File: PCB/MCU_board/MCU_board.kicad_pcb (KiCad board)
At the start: 4 copper layers, 73 x 73 mm, 51 parts, among them IC1 NEO-F10N-00B, IC2 TXB0104PWR, IC3 ESP32-S3-WROOM-1-N4R8, IC6 4259-63, IC8 MAX98357AETE+T, J1 DS1013-40SSIB1-B-0, J4 FXP612 (u.FL) 2, J5 FXP612 (u.FL) 1, J6 SIM8055-6-1-14-00-A, J7 FXP612 (u.FL) 1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

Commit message: all my pcb
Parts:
- removed C10: CL10B104KO8NNNC, CL10B104KO8NNNC:CAPC1608X90N
- moved C2 0.10 mm to (49.0, 138.3)
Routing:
- net /Stationary/GSM_sheet/SIM_POWER: track 37.0 -> 31.0 mm, vias 3 -> 2
- net GND: track 135.6 -> 134.0 mm, vias 36 -> 35

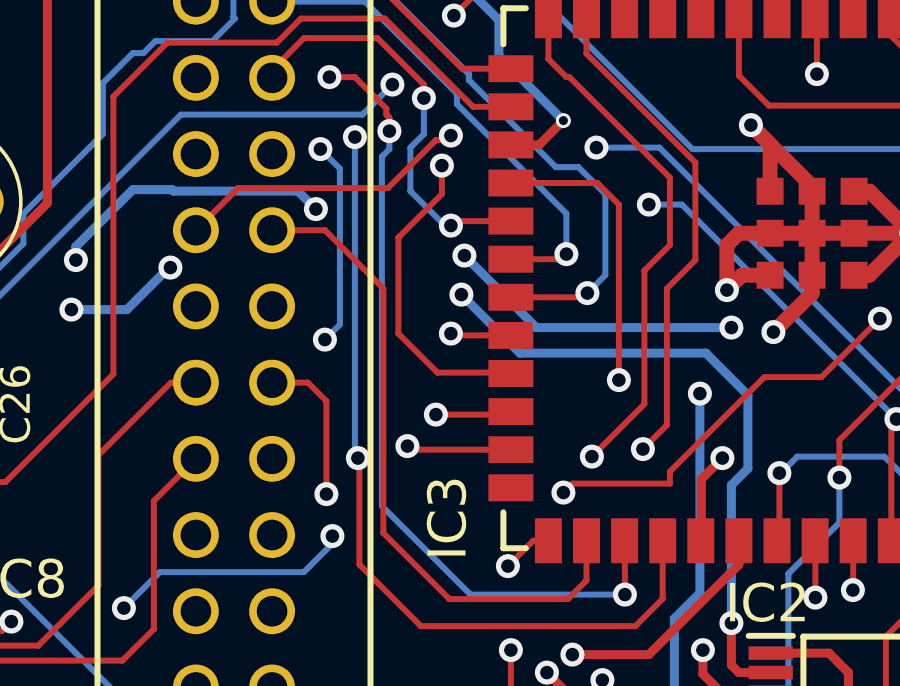
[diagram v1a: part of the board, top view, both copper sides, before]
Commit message: ATA connector updated
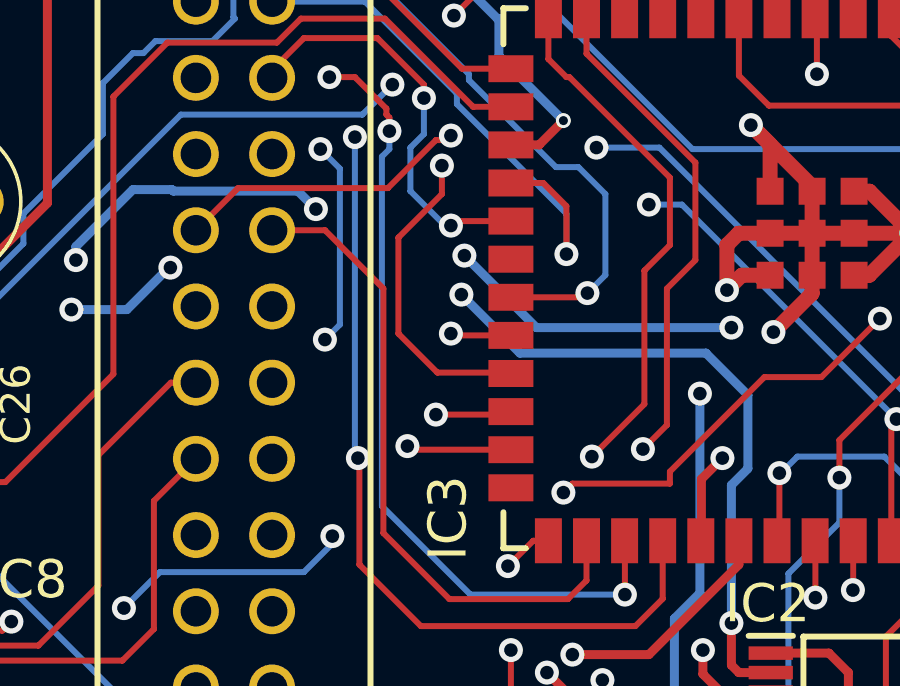
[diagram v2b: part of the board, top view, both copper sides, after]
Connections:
- net /BCLK renamed /SDX
- IC3 pad 18: /WCLK -> /SCX
- IC3 pad 20: /DATA_IN -> unconnected-(IC3-IO12-Pad20)
- J1 pad 16: /DATA_IN -> /SCX
- J1 pad 26: /WCLK -> unconnected-(J1-Pad26)
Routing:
- net /WCLK: track 26.2 -> 0.00 mm, vias 2 -> 0
- net /SCX: track 0.00 -> 18.3 mm, vias 0 -> 1
- net /DATA_IN: track 16.2 -> 0.00 mm, vias 1 -> 0
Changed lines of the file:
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@@
 			(size 0.9 1.5)
 			(layers "F.Cu" "F.Mask" "F.Paste")
-			(net "/WCLK")
+			(net "/SCX")
 			(pinfunction "IO10_18")
 			(pintype "passive")
@@
 			(size 0.9 1.5)
 			(layers "F.Cu" "F.Mask" "F.Paste")
-			(net "/BCLK")
+			(net "/SDX")
 			(pinfunction "IO11_19")
 			(pintype "passive")
@@
 			(size 0.9 1.5)
 			(layers "F.Cu" "F.Mask" "F.Paste")
-			(net "/DATA_IN")
+			(net "unconnected-(IC3-IO12-Pad20)")
 			(pinfunction "IO12_20")
-			(pintype "passive")
+			(pintype "passive+no_connect")
 		)
 		(pad "21" smd rect
@@
 			(layers "*.Cu" "*.Mask")
 			(remove_unused_layers no)
-			(net "/DATA_IN")
+			(net "/SCX")
 			(pinfunction "16_16")
 			(pintype "passive")
@@
 			(layers "*.Cu" "*.Mask")
 			(remove_unused_layers no)
-			(net "/BCLK")
+			(net "/SDX")
 			(pinfunction "18_18")
 			(pintype "passive")
@@
 			(layers "*.Cu" "*.Mask")
 			(remove_unused_layers no)
-			(net "/WCLK")
+			(net "unconnected-(J1-Pad26)")
 			(pinfunction "26_26")
-			(pintype "passive")
+			(pintype "passive+no_connect")
 		)
 		(pad "27" thru_hole circle
@@
 	)
 	(segment
-		(start 81 133.38)
-		(end 83.88 133.38)
-		(width 0.2)
-		(layer "F.Cu")
-		(net "/WCLK")
-	)
-	(segment
-		(start 84.6 134.1)
-		(end 84.6 139.95)
-		(width 0.2)
-		(layer "F.Cu")
-		(net "/WCLK")
-	)
-	(segment
-		(start 73.04 140.035)
-		(end 74.235 140.035)
-		(width 0.2)
-		(layer "F.Cu")
-		(net "/WCLK")
-	)
-	(segment
-		(start 74.235 140.035)
-		(end 74.85 140.65)
-		(width 0.2)
-		(layer "F.Cu")
-		(net "/WCLK")
-	)
-	(segment
-		(start 83.88 133.38)
-		(end 84.6 134.1)
-		(width 0.2)
-		(layer "F.Cu")
-		(net "/WCLK")
-	)
-	(segment
-		(start 74.85 140.65)
-		(end 74.85 143.75)
-		(width 0.2)
-		(layer "F.Cu")
-		(net "/WCLK")
-	)
-	(via
-		(at 84.6 139.95)
-		(size 0.8)
-		(drill 0.45)
-		(layers "F.Cu" "B.Cu")
-		(net "/WCLK")
-	)
-	(via
-		(at 74.85 143.75)
-		(size 0.8)
-		(drill 0.45)
-		(layers "F.Cu" "B.Cu")
-		(net "/WCLK")
-	)
-	(segment
-		(start 74.85 143.75)
-		(end 80.8 143.75)
-		(width 0.2)
-		(layer "In2.Cu")
-		(net "/WCLK")
-	)
-	(segment
-		(start 80.8 143.75)
-		(end 84.6 139.95)
-		(width 0.2)
-		(layer "In2.Cu")
-		(net "/WCLK")
-	)
-	(segment
-		(start 73.04 129.875)
-		(end 73.04 129.61)
-		(width 0.2)
-		(layer "F.Cu")
-		(net "/BCLK")
-	)
-	(segment
-		(start 81 134.65)
-		(end 79.15 134.65)
-		(width 0.2)
-		(layer "F.Cu")
-		(net "/BCLK")
-	)
-	(segment
-		(start 76.55 128.55)
-		(end 78.1 130.1)
-		(width 0.2)
-		(layer "F.Cu")
-		(net "/BCLK")
-	)
-	(segment
-		(start 74.1 128.55)
-		(end 76.55 128.55)
-		(width 0.2)
-		(layer "F.Cu")
-		(net "/BCLK")
-	)
-	(segment
-		(start 78.1 130.1)
-		(end 78.1 130.55)
-		(width 0.2)
-		(layer "F.Cu")
-		(net "/BCLK")
-	)
-	(segment
-		(start 79.15 134.65)
-		(end 79 134.8)
-		(width 0.2)
-		(layer "F.Cu")
-		(net "/BCLK")
-	)
-	(segment
-		(start 73.04 129.61)
-		(end 74.1 128.55)
-		(width 0.2)
-		(layer "F.Cu")
-		(net "/BCLK")
-	)
-	(via
-		(at 79 134.8)
-		(size 0.8)
-		(drill 0.45)
-		(layers "F.Cu" "B.Cu")
-		(net "/BCLK")
-	)
-	(via
-		(at 78.1 130.55)
-		(size 0.8)
-		(drill 0.45)
-		(layers "F.Cu" "B.Cu")
-		(net "/BCLK")
-	)
-	(segment
-		(start 78.1 131.75)
-		(end 77.65 132.2)
-		(width 0.2)
-		(layer "B.Cu")
-		(net "/BCLK")
-	)
-	(segment
-		(start 77.65 132.2)
-		(end 77.65 133.65)
-		(width 0.2)
-		(layer "B.Cu")
-		(net "/BCLK")
-	)
-	(segment
-		(start 78.8 134.8)
-		(end 79 134.8)
-		(width 0.2)
-		(layer "B.Cu")
-		(net "/BCLK")
-	)
-	(segment
-		(start 77.65 133.65)
-		(end 78.8 134.8)
-		(width 0.2)
-		(layer "B.Cu")
-		(net "/BCLK")
-	)
-	(segment
-		(start 78.1 130.55)
-		(end 78.1 131.75)
-		(width 0.2)
-		(layer "B.Cu")
-		(net "/BCLK")
-	)
-	(segment
-		(start 82.68 135.92)
-		(end 82.85 135.75)
-		(width 0.2)
-		(layer "F.Cu")
-		(net "/DATA_IN")
-	)
-	(segment
-		(start 81 135.92)
-		(end 82.68 135.92)
-		(width 0.2)
-		(layer "F.Cu")
-		(net "/DATA_IN")
-	)
-	(via
-		(at 82.85 135.75)
-		(size 0.8)
-		(drill 0.45)
-		(layers "F.Cu" "B.Cu")
-		(net "/DATA_IN")
-	)
-	(segment
-		(start 82.85 135.75)
-		(end 82.85 134.4)
-		(width 0.2)
-		(layer "B.Cu")
-		(net "/DATA_IN")
-	)
-	(segment
-		(start 79.2 130.4)
-		(end 76.135 127.335)
-		(width 0.2)
-		(layer "B.Cu")
-		(net "/DATA_IN")
-	)
-	(segment
-		(start 82.85 134.4)
-		(end 79.2 130.75)
-		(width 0.2)
-		(layer "B.Cu")
-		(net "/DATA_IN")
-	)
-	(segment
-		(start 79.2 130.75)
-		(end 79.2 130.4)
-		(width 0.2)
-		(layer "B.Cu")
-		(net "/DATA_IN")
-	)
-	(segment
-		(start 76.135 127.335)
-		(end 73.04 127.335)
-		(width 0.2)
-		(layer "B.Cu")
-		(net "/DATA_IN")
-	)
-	(segment
 		(start 83.41 137.19)
 		(end 83.55 137.05)
@@
 		(net "Net-(IC1-RESET_N)")
 	)
+	(segment
+		(start 82.85 134.15)
+		(end 82.08 133.38)
+		(width 0.2)
+		(layer "F.Cu")
+		(net "/SCX")
+	)
+	(segment
+		(start 82.68 135.92)
+		(end 82.85 135.75)
+		(width 0.2)
+		(layer "F.Cu")
+		(net "/SCX")
+	)
+	(segment
+		(start 82.08 133.38)
+		(end 81 133.38)
+		(width 0.2)
+		(layer "F.Cu")
+		(net "/SCX")
+	)
+	(segment
+		(start 82.85 135.75)
+		(end 82.85 134.15)
+		(width 0.2)
+		(layer "F.Cu")
+		(net "/SCX")
+	)
+	(via
+		(at 82.85 135.75)
+		(size 0.8)
+		(drill 0.45)
+		(layers "F.Cu" "B.Cu")
+		(net "/SCX")
+	)
+	(segment
+		(start 82.85 135.75)
+		(end 82.85 134.4)
+		(width 0.2)
+		(layer "B.Cu")
+		(net "/SCX")
+	)
+	(segment
+		(start 79.2 130.4)
+		(end 76.135 127.335)
+		(width 0.2)
+		(layer "B.Cu")
+		(net "/SCX")
+	)
+	(segment
+		(start 82.85 134.4)
+		(end 79.2 130.75)
+		(width 0.2)
+		(layer "B.Cu")
+		(net "/SCX")
+	)
+	(segment
+		(start 79.2 130.75)
+		(end 79.2 130.4)
+		(width 0.2)
+		(layer "B.Cu")
+		(net "/SCX")
+	)
+	(segment
+		(start 76.135 127.335)
+		(end 73.04 127.335)
+		(width 0.2)
+		(layer "B.Cu")
+		(net "/SCX")
+	)
+	(segment
+		(start 73.04 129.875)
+		(end 73.04 129.61)
+		(width 0.2)
+		(layer "F.Cu")
+		(net "/SDX")
+	)
+	(segment
+		(start 81 134.65)
+		(end 79.15 134.65)
+		(width 0.2)
+		(layer "F.Cu")
+		(net "/SDX")
+	)
+	(segment
+		(start 76.55 128.55)
+		(end 78.1 130.1)
+		(width 0.2)
+		(layer "F.Cu")
+		(net "/SDX")
+	)
+	(segment
+		(start 74.1 128.55)
+		(end 76.55 128.55)
+		(width 0.2)
+		(layer "F.Cu")
+		(net "/SDX")
+	)
+	(segment
+		(start 78.1 130.1)
+		(end 78.1 130.55)
+		(width 0.2)
+		(layer "F.Cu")
+		(net "/SDX")
+	)
+	(segment
+		(start 79.15 134.65)
+		(end 79 134.8)
+		(width 0.2)
+		(layer "F.Cu")
+		(net "/SDX")
+	)
+	(segment
+		(start 73.04 129.61)
+		(end 74.1 128.55)
+		(width 0.2)
+		(layer "F.Cu")
+		(net "/SDX")
+	)
+	(via
+		(at 79 134.8)
+		(size 0.8)
+		(drill 0.45)
+		(layers "F.Cu" "B.Cu")
+		(net "/SDX")
+	)
+	(via
+		(at 78.1 130.55)
+		(size 0.8)
+		(drill 0.45)
+		(layers "F.Cu" "B.Cu")
+		(net "/SDX")
+	)
+	(segment
+		(start 78.1 131.75)
+		(end 77.65 132.2)
+		(width 0.2)
+		(layer "B.Cu")
+		(net "/SDX")
+	)
+	(segment
+		(start 77.65 132.2)
+		(end 77.65 133.65)
+		(width 0.2)
+		(layer "B.Cu")
+		(net "/SDX")
+	)
+	(segment
+		(start 78.8 134.8)
+		(end 79 134.8)
+		(width 0.2)
+		(layer "B.Cu")
+		(net "/SDX")
+	)
+	(segment
+		(start 77.65 133.65)
+		(end 78.8 134.8)
+		(width 0.2)
+		(layer "B.Cu")
+		(net "/SDX")
+	)
+	(segment
+		(start 78.1 130.55)
+		(end 78.1 131.75)
+		(width 0.2)
+		(layer "B.Cu")
+		(net "/SDX")
+	)
 	(zone

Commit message: modified gnd
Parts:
- removed IC8: MAX98357AETE+T, MAX98357AETE+T:QFN50P300X300X80-17N
- removed R16, R26: 100kΩ, Resistor_THT:R_Axial_DIN0207_L6.3mm_D2.5mm_P7.62mm_Horizontal
- added IC4: MAX98357AETE+T, MAX98357AETE+T:QFN50P300X300X80-17N, F.Cu at (61.8, 148.6)
- added J2: Conn_02x04_Counter_Clockwise, Connector_PinHeader_2.54mm:PinHeader_2x04_P2.54mm_Vertical, F.Cu at (34.8, 153.7)
- added R1: 10kΩ, Resistor_SMD:R_0603_1608Metric, F.Cu at (57.4, 147.0)
- added R2: 100kΩ, Resistor_SMD:R_0603_1608Metric, F.Cu at (54.7, 146.8)
- C1: footprint Capacitor_THT:C_Disc_D5.0mm_W2.5mm_P2.50mm -> Capacitor_SMD:CP_Elec_6.3x5.4; moved to B.Cu
- C12, C13, C2, C22, C26, C3, C8: footprint Capacitor_THT:C_Disc_D5.0mm_W2.5mm_P2.50mm -> Capacitor_SMD:CP_Elec_6.3x5.4
- C23, C24, C25, C4: footprint Capacitor_THT:CP_Radial_Tantal_D5.0mm_P2.50mm -> Capacitor_Tantalum_SMD:CP_EIA-3216-18_Kemet-A
- D4: footprint Diode_THT:D_DO-41_SOD81_P7.62mm_Horizontal -> LED_SMD:LED_0603_1608Metric; moved to B.Cu
- Q3: footprint Si2323DDS-T1-GE3:SOT95P237X112-3N -> Package_TO_SOT_SMD:SOT-23
- R17, R19, R20, R21, R28, R29, R30: footprint Resistor_THT:R_Axial_DIN0207_L6.3mm_D2.5mm_P7.62mm_Horizontal -> Resistor_SMD:R_0603_1608Metric
- R18: footprint Resistor_THT:R_Axial_DIN0207_L6.3mm_D2.5mm_P7.62mm_Horizontal -> Resistor_SMD:R_0603_1608Metric; moved to B.Cu
- moved R21 55.5 mm to (47.8, 143.8), turned to -90 degrees
- moved C12 54.1 mm to (41.1, 145.7), turned to 90 degrees
- moved R20 50.5 mm to (53.3, 139.8), turned to 90 degrees
- moved C13 40.2 mm to (45.6, 136.6)
- moved C24 39.3 mm to (67.0, 166.3), turned to -90 degrees
- moved J7 38.9 mm to (55.6, 134.9)
- moved C25 32.2 mm to (57.0, 163.3), turned to -90 degrees
- moved C26 24.8 mm to (61.9, 164.3)
- moved R18 22.3 mm to (52.4, 127.5), turned to 0 degrees
- moved C22 22.1 mm to (61.2, 155.4)
- moved C3 17.6 mm to (83.7, 106.8)
- moved R17 15.4 mm to (94.7, 109.7), turned to 0 degrees
- moved C2 13.2 mm to (35.7, 138.3)
- moved D4 11.4 mm to (48.6, 127.4)
- moved C1 9.39 mm to (89.2, 106.3)
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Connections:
- net /3V8 renamed BAT+
- J1 pad 23: /BAT+ -> unconnected-(J1-Pad23)
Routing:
- net GND: track 134.0 -> 171.5 mm, vias 35 -> 47
- net /TIMEPULSE: track 76.2 -> 95.4 mm, vias 6 -> 7
- net /TXD: track 88.4 -> 106.3 mm
- net /RXD: track 86.9 -> 104.0 mm
- net /+3V3: track 181.3 -> 198.1 mm, vias 4 -> 6
- net Net-(IC8-GAIN_SLOT): track 16.2 -> 0.00 mm, vias 1 -> 0
- net /GSM_POWER: track 3.04 -> 19.2 mm, vias 0 -> 2
- net Net-(U2-VBAT@1): track 76.4 -> 91.9 mm, vias 1 -> 3
- net Net-(D4-K): track 14.7 -> 1.67 mm
- net Net-(U2-RF_ANT): track 47.2 -> 36.9 mm
- net Net-(IC8-~{SD_MODE}): track 7.52 -> 0.00 mm
- net Net-(Q3-G): track 7.31 -> 14.7 mm
- net /Stationary/GSM_sheet/SIM_POWER: track 31.0 -> 24.0 mm
- net Net-(IC4-~{SD_MODE}): track 0.00 -> 6.71 mm
- net /LOUDNESS: track 78.2 -> 84.5 mm, vias 2 -> 3
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
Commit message: bought pcbs
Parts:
- C2: moved to B.Cu
- J6: moved to F.Cu
- moved C2 21.8 mm to (43.2, 117.8), turned to 180 degrees
- moved J6 19.7 mm to (35.7, 137.6)
- moved C12 9.20 mm to (50.3, 145.8)
- moved TP3 9.08 mm to (32.1, 123.3)
- moved TP1 7.96 mm to (32.2, 118.9)
- moved R21 6.48 mm to (52.6, 139.5)
- moved C13 2.43 mm to (48.0, 136.6)
- moved R20 1.91 mm to (55.2, 139.6)
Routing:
- net Net-(U2-USB_DM): track 22.1 -> 6.26 mm
- net /Stationary/GSM_sheet/CARD_DETECT: track 8.72 -> 19.5 mm, vias 1 -> 0
- net Net-(C12-Pad2): track 14.6 -> 6.22 mm
- net Net-(U2-USB_DP): track 11.0 -> 4.88 mm
- net /Stationary/GSM_sheet/SIM_POWER: track 24.0 -> 29.8 mm, vias 2 -> 3
- net GND: track 171.5 -> 165.8 mm, vias 47 -> 48
- net /Stationary/GSM_sheet/SIM_RST: track 13.4 -> 18.7 mm, vias 1 -> 2
- net Net-(U2-RF_ANT): track 36.9 -> 32.0 mm
- net /Stationary/GSM_sheet/SIM_DATA: track 11.4 -> 15.3 mm, vias 1 -> 0
- net /Stationary/GSM_sheet/SIM_CLK: track 13.4 -> 14.9 mm, vias 2 -> 0
- net Net-(J7-In): track 3.53 -> 2.52 mm
